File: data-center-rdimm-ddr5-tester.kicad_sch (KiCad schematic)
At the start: 2 parts

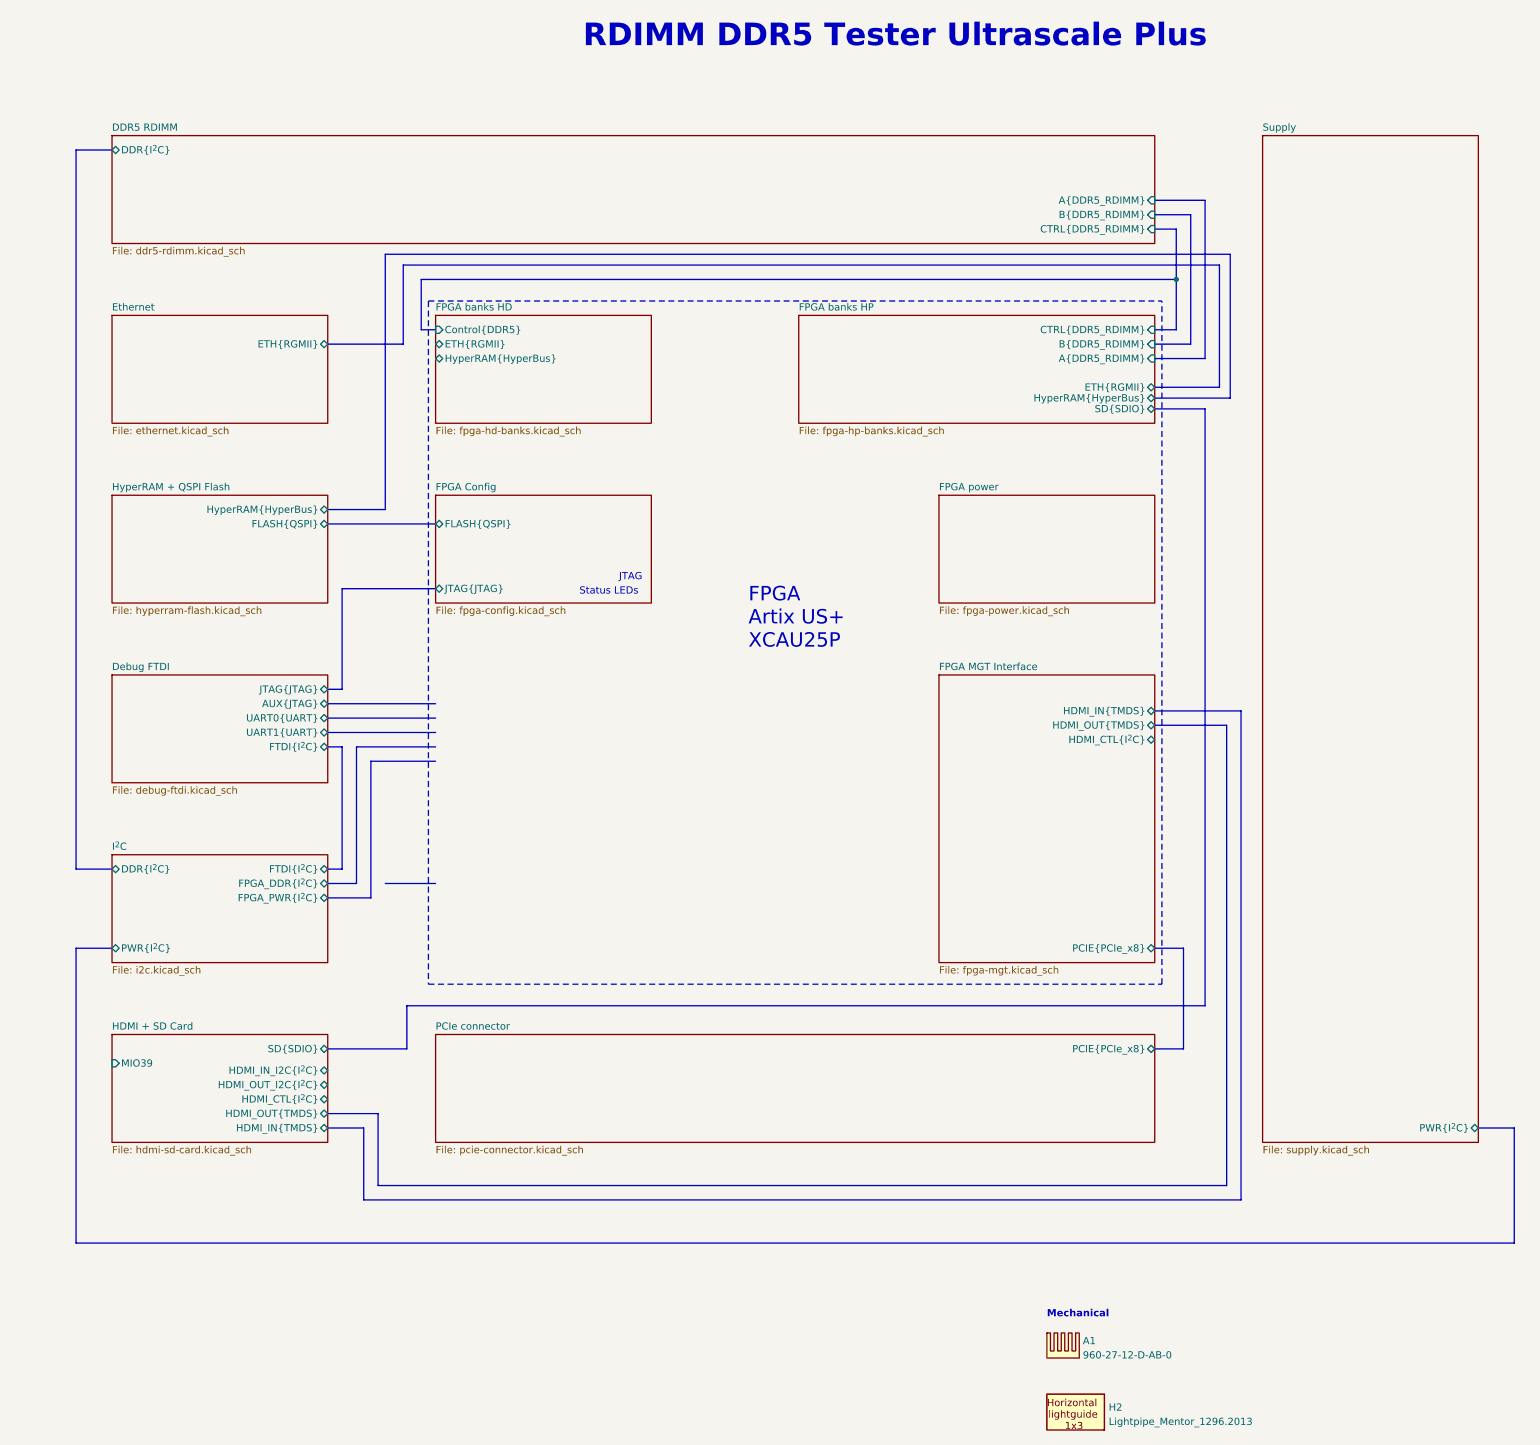
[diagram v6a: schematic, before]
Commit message: [#66312] Connected LS HDMI signals
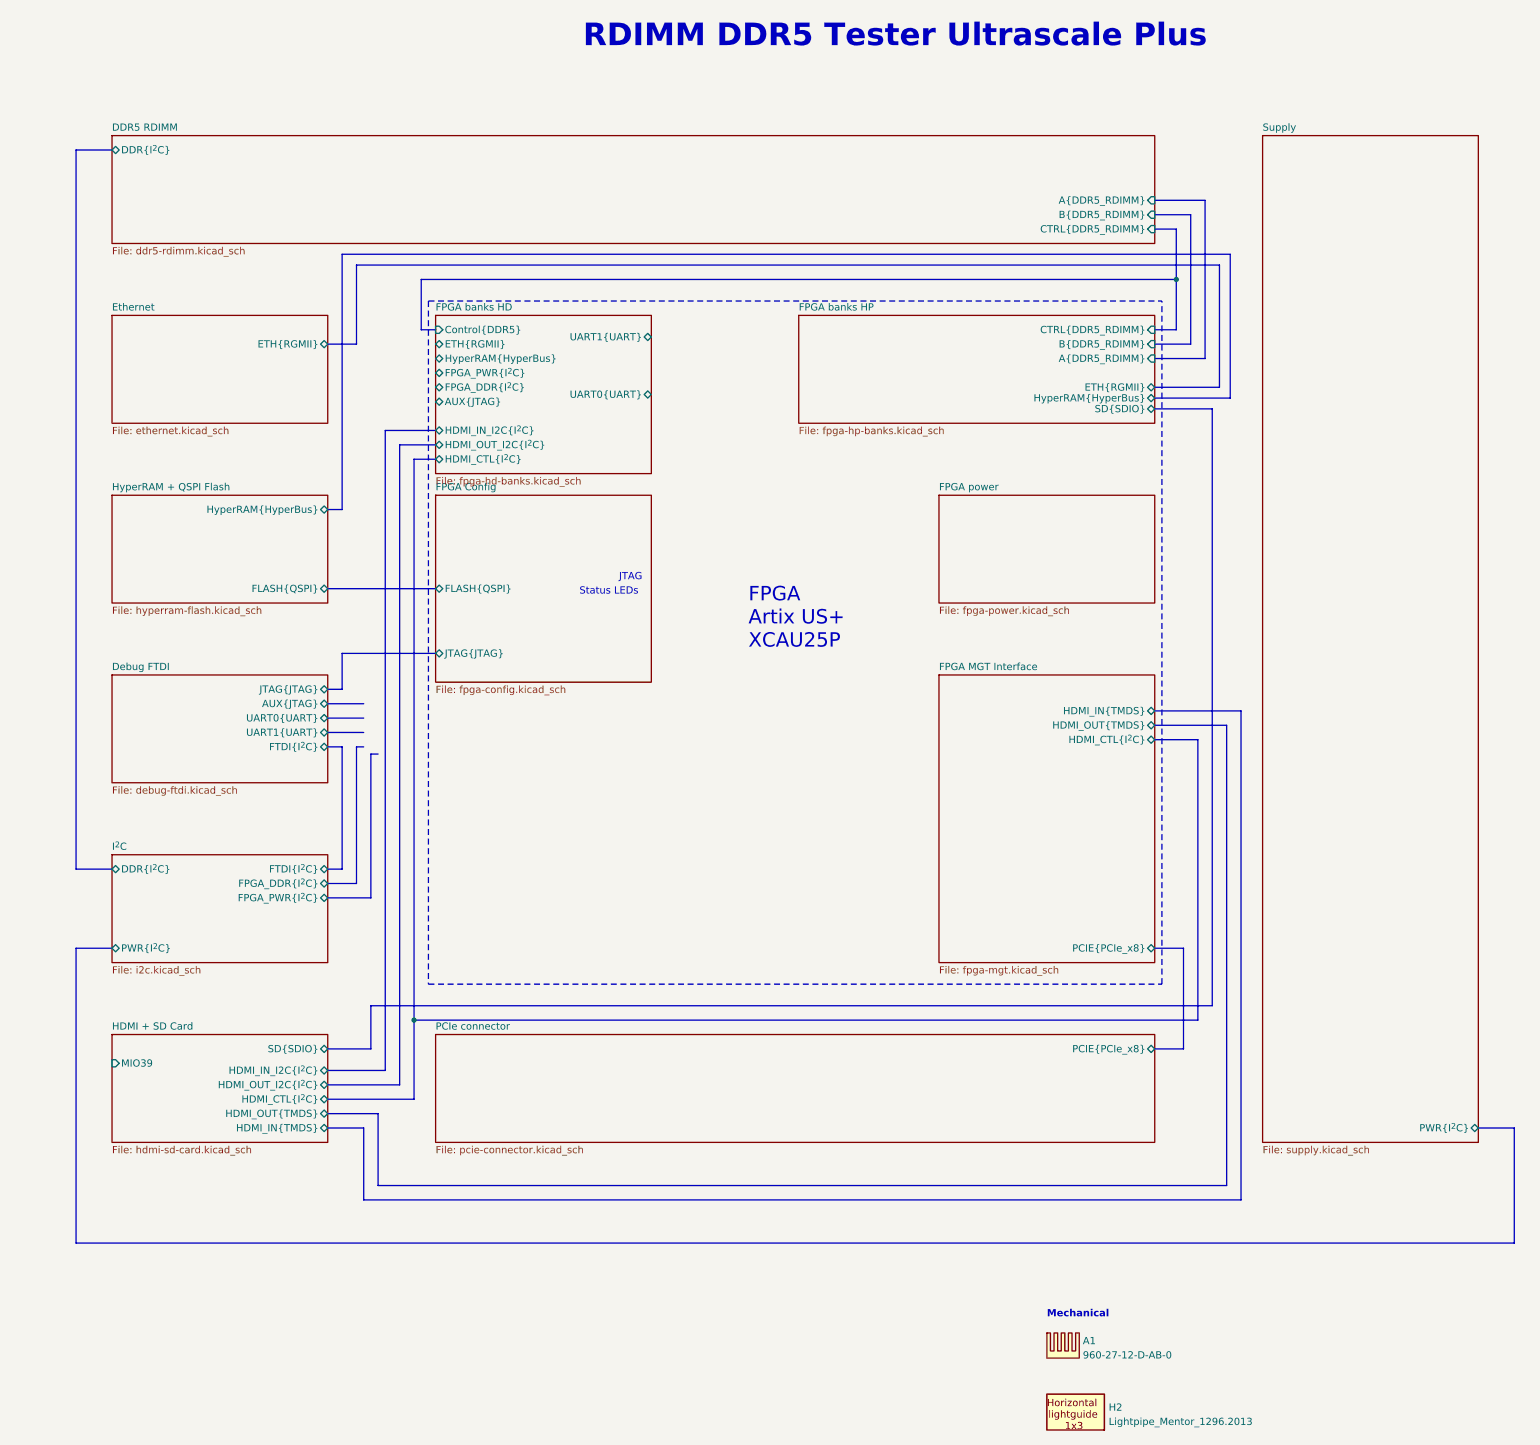
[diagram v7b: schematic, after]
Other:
- sheet FPGA banks HD ports: added AUX{JTAG}, FPGA_DDR{I^{2}C}, FPGA_PWR{I^{2}C}, HDMI_CTL{I^{2}C}, HDMI_IN_I2C{I^{2}C}, HDMI_OUT_I2C{I^{2}C}, UART0{UART}, UART1{UART}; removed none
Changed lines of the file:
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@@
   (junction (at 276.86 76.2) (diameter 0) (color 0 0 0 0)
+  )
+  (junction (at 142.24 207.01) (diameter 0) (color 0 0 0 0)
   )
   (bus (pts (xy 286.385 97.155) (xy 286.385 71.755))
     (stroke (width 0) (type default) (color 208 190 93 1))
   )
-  (bus (pts (xy 127 153.67) (xy 146.05 153.67))
-    (stroke (width 0) (type default))
-  )
-  (bus (pts (xy 140.335 87.63) (xy 140.335 73.66))
+  (bus (pts (xy 132.08 87.63) (xy 132.08 73.66))
     (stroke (width 0) (type default) (color 210 55 51 1))
   )
@@
     (stroke (width 0) (type default))
   )
-  (bus (pts (xy 127 212.09) (xy 140.97 212.09))
+  (bus (pts (xy 127 212.09) (xy 134.62 212.09))
     (stroke (width 0) (type default) (color 205 115 190 1))
   )
-  (bus (pts (xy 146.05 182.88) (xy 137.16 182.88))
-    (stroke (width 0) (type default))
-  )
   (bus (pts (xy 146.05 85.09) (xy 143.51 85.09))
     (stroke (width 0) (type default))
@@
     (stroke (width 0) (type default))
   )
-  (bus (pts (xy 146.05 130.81) (xy 129.54 130.81))
+  (bus (pts (xy 146.05 142.24) (xy 129.54 142.24))
+    (stroke (width 0) (type default))
+  )
+  (bus (pts (xy 137.16 215.9) (xy 127 215.9))
+    (stroke (width 0) (type default))
+  )
+  (bus (pts (xy 280.67 207.01) (xy 280.67 157.48))
     (stroke (width 0) (type default))
   )
@@
     (stroke (width 0) (type default))
   )
-  (bus (pts (xy 140.335 73.66) (xy 284.48 73.66))
+  (bus (pts (xy 142.24 207.01) (xy 142.24 220.98))
+    (stroke (width 0) (type default))
+  )
+  (bus (pts (xy 132.08 73.66) (xy 284.48 73.66))
     (stroke (width 0) (type default) (color 210 55 51 1))
   )
@@
     (stroke (width 0) (type default))
   )
-  (bus (pts (xy 137.16 71.755) (xy 137.16 116.84))
+  (bus (pts (xy 129.54 71.755) (xy 129.54 116.84))
     (stroke (width 0) (type default) (color 208 190 93 1))
   )
+  (bus (pts (xy 134.62 160.02) (xy 135.89 160.02))
+    (stroke (width 0) (type default))
+  )
   (bus (pts (xy 279.4 87.63) (xy 273.05 87.63))
     (stroke (width 0) (type default))
@@
     (stroke (width 0) (type default))
   )
-  (bus (pts (xy 137.16 116.84) (xy 127 116.84))
+  (bus (pts (xy 129.54 116.84) (xy 127 116.84))
     (stroke (width 0) (type default) (color 208 190 93 1))
   )
@@
     (stroke (width 0) (type default))
   )
-  (bus (pts (xy 127 87.63) (xy 140.335 87.63))
+  (bus (pts (xy 127 87.63) (xy 132.08 87.63))
     (stroke (width 0) (type default) (color 210 55 51 1))
   )
@@
     (stroke (width 0) (type default))
   )
-  (bus (pts (xy 134.62 161.29) (xy 146.05 161.29))
+  (bus (pts (xy 280.67 157.48) (xy 273.05 157.48))
     (stroke (width 0) (type default))
   )
@@
     (stroke (width 0) (type default) (color 208 190 93 1))
   )
+  (bus (pts (xy 142.24 207.01) (xy 280.67 207.01))
+    (stroke (width 0) (type default))
+  )
   (bus (pts (xy 133.35 226.06) (xy 127 226.06))
     (stroke (width 0) (type default))
@@
     (stroke (width 0) (type default))
   )
-  (bus (pts (xy 146.05 158.75) (xy 132.08 158.75))
-    (stroke (width 0) (type default))
-  )
   (bus (pts (xy 285.75 154.94) (xy 273.05 154.94))
     (stroke (width 0) (type default))
   )
-  (bus (pts (xy 129.54 130.81) (xy 129.54 148.59))
+  (bus (pts (xy 129.54 142.24) (xy 129.54 148.59))
+    (stroke (width 0) (type default))
+  )
+  (bus (pts (xy 132.08 158.75) (xy 133.35 158.75))
     (stroke (width 0) (type default))
   )
@@
     (stroke (width 0) (type default))
   )
-  (bus (pts (xy 127 119.38) (xy 146.05 119.38))
+  (bus (pts (xy 127 218.44) (xy 139.7 218.44))
     (stroke (width 0) (type default))
   )
@@
     (stroke (width 0) (type default))
   )
+  (bus (pts (xy 139.7 105.41) (xy 146.05 105.41))
+    (stroke (width 0) (type default))
+  )
   (bus (pts (xy 127 158.75) (xy 129.54 158.75))
     (stroke (width 0) (type default))
@@
     (stroke (width 0) (type default))
   )
+  (bus (pts (xy 142.24 107.95) (xy 142.24 207.01))
+    (stroke (width 0) (type default))
+  )
   (bus (pts (xy 276.86 85.09) (xy 273.05 85.09))
     (stroke (width 0) (type default))
   )
-  (bus (pts (xy 127 156.21) (xy 146.05 156.21))
-    (stroke (width 0) (type default))
-  )
-  (bus (pts (xy 281.94 99.06) (xy 281.94 204.47))
+  (bus (pts (xy 283.21 99.06) (xy 283.21 204.47))
     (stroke (width 0) (type default) (color 205 115 190 1))
   )
@@
     (stroke (width 0) (type default))
   )
-  (bus (pts (xy 281.94 99.06) (xy 273.05 99.06))
+  (bus (pts (xy 283.21 99.06) (xy 273.05 99.06))
     (stroke (width 0) (type default) (color 205 115 190 1))
   )
+  (bus (pts (xy 142.24 220.98) (xy 127 220.98))
+    (stroke (width 0) (type default))
+  )
   (bus (pts (xy 278.13 194.31) (xy 278.13 212.09))
     (stroke (width 0) (type default))
@@
     (stroke (width 0) (type default))
   )
-  (bus (pts (xy 127 151.13) (xy 146.05 151.13))
-    (stroke (width 0) (type default))
-  )
-  (bus (pts (xy 286.385 71.755) (xy 137.16 71.755))
+  (bus (pts (xy 137.16 102.87) (xy 137.16 215.9))
+    (stroke (width 0) (type default))
+  )
+  (bus (pts (xy 127 153.67) (xy 133.35 153.67))
+    (stroke (width 0) (type default))
+  )
+  (bus (pts (xy 286.385 71.755) (xy 129.54 71.755))
     (stroke (width 0) (type default) (color 208 190 93 1))
+  )
+  (bus (pts (xy 139.7 218.44) (xy 139.7 105.41))
+    (stroke (width 0) (type default))
+  )
+  (bus (pts (xy 146.05 107.95) (xy 142.24 107.95))
+    (stroke (width 0) (type default))
   )
   (bus (pts (xy 284.48 95.25) (xy 273.05 95.25))
     (stroke (width 0) (type default) (color 210 55 51 1))
   )
-  (bus (pts (xy 140.97 204.47) (xy 140.97 212.09))
+  (bus (pts (xy 134.62 204.47) (xy 134.62 212.09))
     (stroke (width 0) (type default) (color 205 115 190 1))
   )
@@
     (stroke (width 0) (type default))
   )
-  (bus (pts (xy 140.97 204.47) (xy 281.94 204.47))
+  (bus (pts (xy 134.62 204.47) (xy 283.21 204.47))
     (stroke (width 0) (type default) (color 205 115 190 1))
+  )
+  (bus (pts (xy 146.05 102.87) (xy 137.16 102.87))
+    (stroke (width 0) (type default))
   )
   (polyline (pts (xy 144.78 80.01) (xy 144.78 200.66))
@@
     (stroke (width 0) (type default))
   )
-  (bus (pts (xy 134.62 185.42) (xy 134.62 161.29))
+  (bus (pts (xy 134.62 160.02) (xy 134.62 185.42))
     (stroke (width 0) (type default))
   )
@@
     (stroke (width 0) (type default))
   )
+  (bus (pts (xy 127 156.21) (xy 133.35 156.21))
+    (stroke (width 0) (type default))
+  )
+  (bus (pts (xy 127 130.81) (xy 146.05 130.81))
+    (stroke (width 0) (type default))
+  )
   (bus (pts (xy 127 223.52) (xy 135.89 223.52))
+    (stroke (width 0) (type default))
+  )
+  (bus (pts (xy 127 151.13) (xy 133.35 151.13))
     (stroke (width 0) (type default))
   )
@@
     )
   )
-  (sheet (at 146.05 114.3) (size 38.1 19.05) (fields_autoplaced)
+  (sheet (at 146.05 114.3) (size 38.1 33.02) (fields_autoplaced)
     (stroke (width 0) (type solid))
     (fill (color 0 0 0 0.0000))
@@
       (effects (font (size 1.27 1.27)) (justify left bottom))
     )
-    (property "Sheetfile" "fpga-config.kicad_sch" (at 146.05 133.9346 0)
+    (property "Sheetfile" "fpga-config.kicad_sch" (at 146.05 147.9046 0)
       (effects (font (size 1.27 1.27)) (justify left top))
     )
-    (pin "JTAG{JTAG}" bidirectional (at 146.05 130.81 180)
+    (pin "JTAG{JTAG}" bidirectional (at 146.05 142.24 180)
       (effects (font (size 1.27 1.27)) (justify left))
     )
-    (pin "FLASH{QSPI}" bidirectional (at 146.05 119.38 180)
+    (pin "FLASH{QSPI}" bidirectional (at 146.05 130.81 180)
       (effects (font (size 1.27 1.27)) (justify left))
     )
@@
       (effects (font (size 1.27 1.27)) (justify right))
     )
-    (pin "FLASH{QSPI}" bidirectional (at 127 119.38 0)
+    (pin "FLASH{QSPI}" bidirectional (at 127 130.81 0)
       (effects (font (size 1.27 1.27)) (justify right))
     )
@@
     )
   )
-  (sheet (at 146.05 82.55) (size 38.1 19.05) (fields_autoplaced)
+  (sheet (at 146.05 82.55) (size 38.1 27.94) (fields_autoplaced)
     (stroke (width 0.1524) (type solid))
     (fill (color 0 0 0 0.0000))
@@
       (effects (font (size 1.27 1.27)) (justify left bottom))
     )
-    (property "Sheetfile" "fpga-hd-banks.kicad_sch" (at 146.05 102.1846 0)
+    (property "Sheetfile" "fpga-hd-banks.kicad_sch" (at 146.05 111.0746 0)
       (effects (font (size 1.27 1.27)) (justify left top))
     )
@@
       (effects (font (size 1.27 1.27)) (justify left))
     )
+    (pin "FPGA_PWR{I^{2}C}" bidirectional (at 146.05 92.71 180)
+      (effects (font (size 1.27 1.27)) (justify left))
+    )
+    (pin "FPGA_DDR{I^{2}C}" bidirectional (at 146.05 95.25 180)
+      (effects (font (size 1.27 1.27)) (justify left))
+    )
+    (pin "AUX{JTAG}" bidirectional (at 146.05 97.79 180)
+      (effects (font (size 1.27 1.27)) (justify left))
+    )
+    (pin "UART1{UART}" bidirectional (at 184.15 86.36 0)
+      (effects (font (size 1.27 1.27)) (justify right))
+    )
+    (pin "HDMI_OUT_I2C{I^{2}C}" bidirectional (at 146.05 105.41 180)
+      (effects (font (size 1.27 1.27)) (justify left))
+    )
+    (pin "HDMI_CTL{I^{2}C}" bidirectional (at 146.05 107.95 180)
+      (effects (font (size 1.27 1.27)) (justify left))
+    )
+    (pin "UART0{UART}" bidirectional (at 184.15 96.52 0)
+      (effects (font (size 1.27 1.27)) (justify right))
+    )
+    (pin "HDMI_IN_I2C{I^{2}C}" bidirectional (at 146.05 102.87 180)
+      (effects (font (size 1.27 1.27)) (justify left))
+    )
